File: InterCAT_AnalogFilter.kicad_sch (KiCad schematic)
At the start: 37 parts, among them T1 Transformer_1P_1S, T2 Transformer_1P_1S, T3 Transformer_1P_1S, T4 Transformer_1P_1S, U4 MCP6002, U5 MCP6002, U6 MCP6002

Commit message: added footprints for trimmers and trasf
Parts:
- RV1, RV2, RV3, RV4: footprint (none) -> Potentiometer_THT:Potentiometer_Bourns_3386P_Vertical
- T1, T2, T3, T4: footprint (none) -> InterCat:LM-NP-1001-B1L
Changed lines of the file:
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@@
       (effects (font (size 1.27 1.27)))
     )
-    (property "Footprint" "" (at 226.06 48.26 0)
+    (property "Footprint" "Potentiometer_THT:Potentiometer_Bourns_3386P_Vertical" (at 226.06 48.26 0)
       (effects (font (size 1.27 1.27)) hide)
     )
@@
       (effects (font (size 1.27 1.27)))
     )
-    (property "Footprint" "" (at 127 43.18 0)
+    (property "Footprint" "InterCat:LM-NP-1001-B1L" (at 127 43.18 0)
       (effects (font (size 1.27 1.27)) hide)
     )
@@
       (effects (font (size 1.27 1.27)))
     )
-    (property "Footprint" "" (at 93.98 101.6 0)
+    (property "Footprint" "Potentiometer_THT:Potentiometer_Bourns_3386P_Vertical" (at 93.98 101.6 0)
       (effects (font (size 1.27 1.27)) hide)
     )
@@
       (effects (font (size 1.27 1.27)))
     )
-    (property "Footprint" "" (at 179.07 101.6 0)
+    (property "Footprint" "InterCat:LM-NP-1001-B1L" (at 179.07 101.6 0)
       (effects (font (size 1.27 1.27)) hide)
     )
@@
       (effects (font (size 1.27 1.27)))
     )
-    (property "Footprint" "" (at 180.34 43.18 0)
+    (property "Footprint" "InterCat:LM-NP-1001-B1L" (at 180.34 43.18 0)
       (effects (font (size 1.27 1.27)) hide)
     )
@@
       (effects (font (size 1.27 1.27)))
     )
-    (property "Footprint" "" (at 224.79 106.68 0)
+    (property "Footprint" "Potentiometer_THT:Potentiometer_Bourns_3386P_Vertical" (at 224.79 106.68 0)
       (effects (font (size 1.27 1.27)) hide)
     )
@@
       (effects (font (size 1.27 1.27)))
     )
-    (property "Footprint" "" (at 93.98 39.37 0)
+    (property "Footprint" "Potentiometer_THT:Potentiometer_Bourns_3386P_Vertical" (at 93.98 39.37 0)
       (effects (font (size 1.27 1.27)) hide)
     )
@@
       (effects (font (size 1.27 1.27)))
     )
-    (property "Footprint" "" (at 127 105.41 0)
-      (effects (font (size 1.27 1.27)) hide)
-    )
+    (property "Footprint" "InterCat:LM-NP-1001-B1L" (at 127 105.41 0)
+      (effects (font (size 1.27 1.27)) hide)
+    )

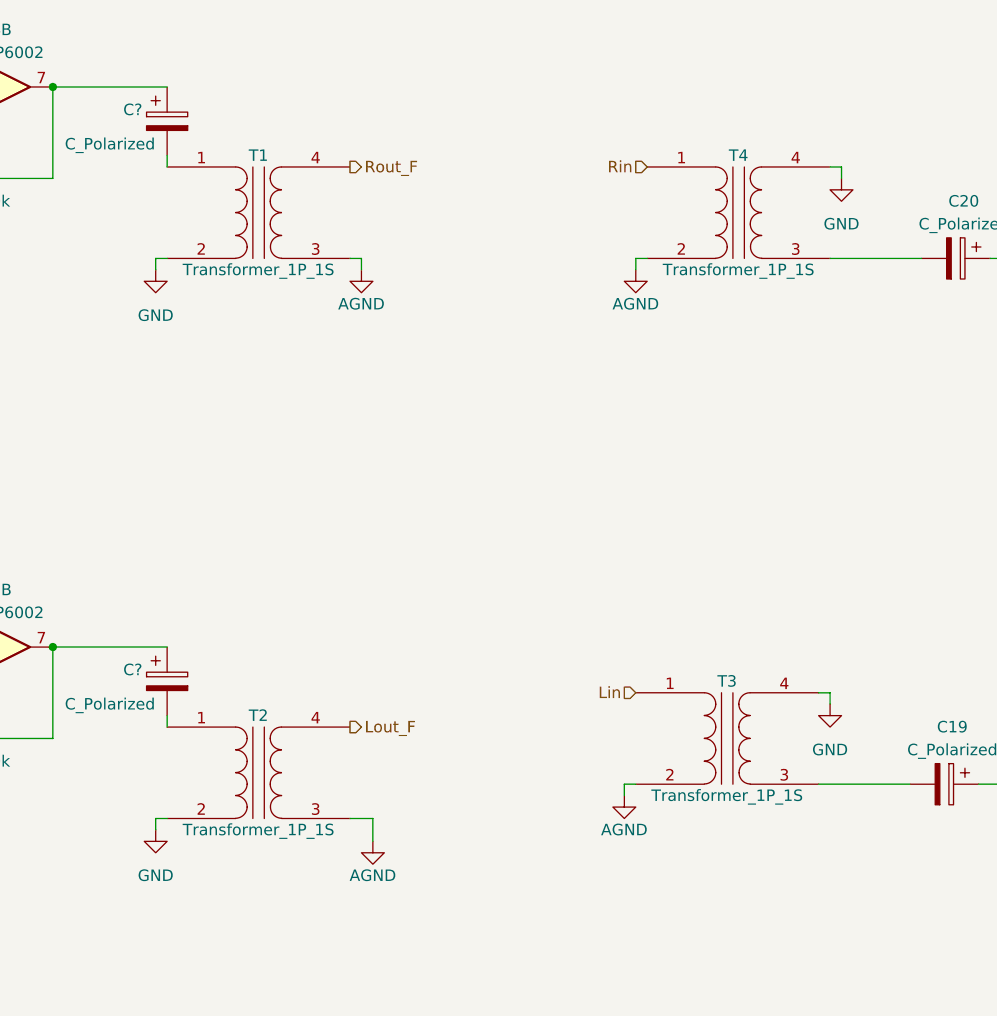
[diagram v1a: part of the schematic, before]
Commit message: corrected footprint AND symbol of trasf
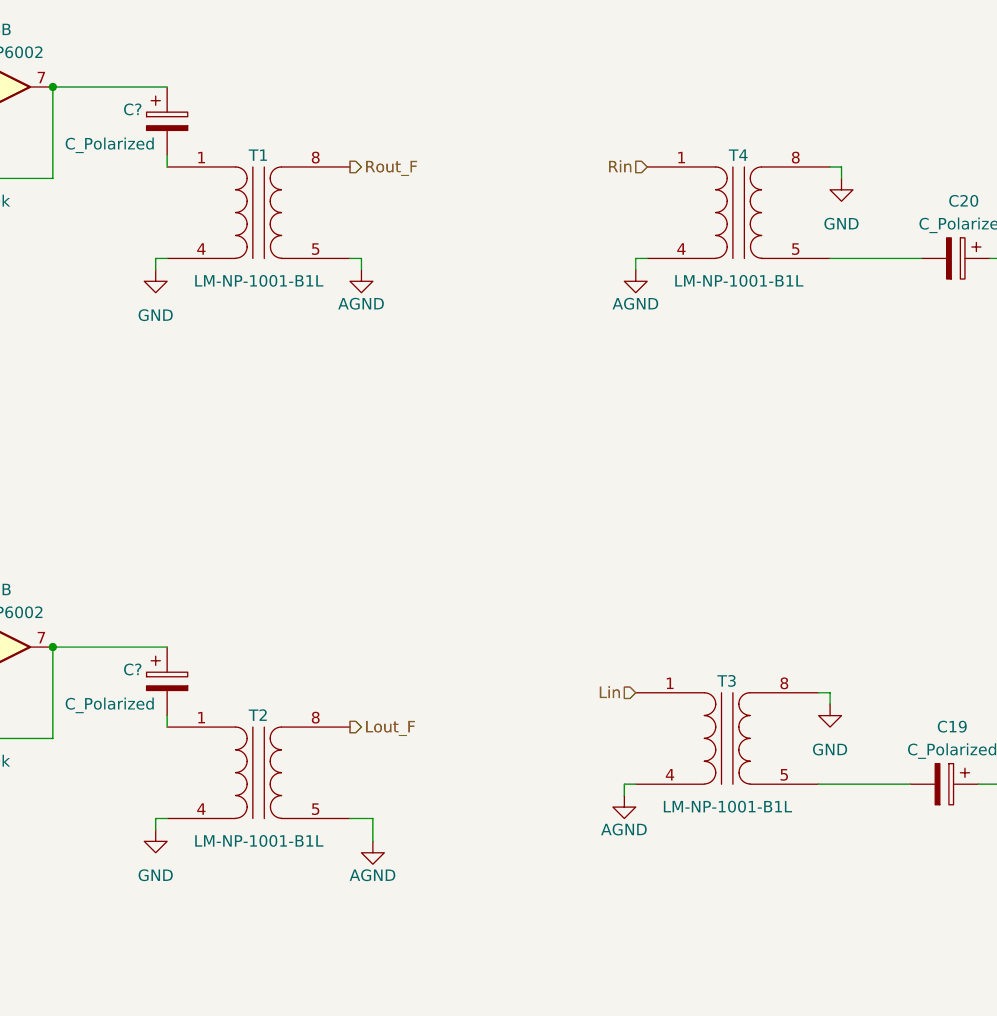
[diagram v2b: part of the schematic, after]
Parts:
- T1, T2, T3, T4: value Transformer_1P_1S -> LM-NP-1001-B1L; symbol Device:Transformer_1P_1S -> InterCat:LM-NP-1001-B1L
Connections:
- net GND: now also T1.4 (AB), T2.4 (AB), T3.8 (SB), T4.8 (SB); no longer T1.2 (AB), T2.2 (AB), T3.4 (SB), T4.4 (SB)
- net GNDA: now also T1.5 (SA), T2.5 (SA), T3.4 (AB), T4.4 (AB); no longer T1.3 (SA), T2.3 (SA), T3.2 (AB), T4.2 (AB)
- net Lout_F: now also T2.8 (SB); no longer T2.4 (SB)
- net Rout_F: now also T1.8 (SB); no longer T1.4 (SB)
- net at C20.2: now also T4.5 (SA); no longer T4.3 (SA)
- net at C19.2: now also T3.5 (SA); no longer T3.3 (SA)
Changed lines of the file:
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@@
     )
   )
-  (symbol (lib_id "Device:Transformer_1P_1S") (at 127 43.18 0) (unit 1)
+  (symbol (lib_id "InterCat:LM-NP-1001-B1L") (at 127 43.18 0) (unit 1)
     (in_bom yes) (on_board yes) (dnp no)
     (property "Reference" "T1" (at 127 36.83 0)
       (effects (font (size 1.27 1.27)))
     )
-    (property "Value" "Transformer_1P_1S" (at 127 49.53 0)
-      (effects (font (size 1.27 1.27)))
-    )
-    (property "Footprint" "InterCat:LM-NP-1001-B1L" (at 127 43.18 0)
-      (effects (font (size 1.27 1.27)) hide)
-    )
-    (property "Datasheet" "~" (at 127 43.18 0)
+    (property "Value" "LM-NP-1001-B1L" (at 127 50.8 0)
+      (effects (font (size 1.27 1.27)))
+    )
+    (property "Footprint" "InterCat:LM-NP-1001-B1L" (at 125.73 43.18 0)
+      (effects (font (size 1.27 1.27)) hide)
+    )
+    (property "Datasheet" "https://www.bourns.com/pdfs/LMNPLP.pdf" (at 127 43.18 0)
       (effects (font (size 1.27 1.27)) hide)
     )
@@
     )
     (pin "1")
-    (pin "2")
-    (pin "3")
     (pin "4")
+    (pin "5")
+    (pin "8")
     (instances
       (project "Intercat"
@@
     )
   )
-  (symbol (lib_id "Device:Transformer_1P_1S") (at 179.07 101.6 0) (unit 1)
+  (symbol (lib_id "InterCat:LM-NP-1001-B1L") (at 179.07 101.6 0) (unit 1)
     (in_bom yes) (on_board yes) (dnp no)
     (property "Reference" "T3" (at 179.07 95.25 0)
       (effects (font (size 1.27 1.27)))
     )
-    (property "Value" "Transformer_1P_1S" (at 179.07 107.95 0)
-      (effects (font (size 1.27 1.27)))
-    )
-    (property "Footprint" "InterCat:LM-NP-1001-B1L" (at 179.07 101.6 0)
-      (effects (font (size 1.27 1.27)) hide)
-    )
-    (property "Datasheet" "~" (at 179.07 101.6 0)
+    (property "Value" "LM-NP-1001-B1L" (at 179.07 109.22 0)
+      (effects (font (size 1.27 1.27)))
+    )
+    (property "Footprint" "InterCat:LM-NP-1001-B1L" (at 177.8 101.6 0)
+      (effects (font (size 1.27 1.27)) hide)
+    )
+    (property "Datasheet" "https://www.bourns.com/pdfs/LMNPLP.pdf" (at 179.07 101.6 0)
       (effects (font (size 1.27 1.27)) hide)
     )
@@
     )
     (pin "1")
-    (pin "2")
-    (pin "3")
     (pin "4")
+    (pin "5")
+    (pin "8")
     (instances
       (project "Intercat"
@@
     )
   )
-  (symbol (lib_id "Device:Transformer_1P_1S") (at 180.34 43.18 0) (unit 1)
+  (symbol (lib_id "InterCat:LM-NP-1001-B1L") (at 180.34 43.18 0) (unit 1)
     (in_bom yes) (on_board yes) (dnp no)
     (property "Reference" "T4" (at 180.34 36.83 0)
       (effects (font (size 1.27 1.27)))
     )
-    (property "Value" "Transformer_1P_1S" (at 180.34 49.53 0)
-      (effects (font (size 1.27 1.27)))
-    )
-    (property "Footprint" "InterCat:LM-NP-1001-B1L" (at 180.34 43.18 0)
-      (effects (font (size 1.27 1.27)) hide)
-    )
-    (property "Datasheet" "~" (at 180.34 43.18 0)
+    (property "Value" "LM-NP-1001-B1L" (at 180.34 50.8 0)
+      (effects (font (size 1.27 1.27)))
+    )
+    (property "Footprint" "InterCat:LM-NP-1001-B1L" (at 179.07 43.18 0)
+      (effects (font (size 1.27 1.27)) hide)
+    )
+    (property "Datasheet" "https://www.bourns.com/pdfs/LMNPLP.pdf" (at 180.34 43.18 0)
       (effects (font (size 1.27 1.27)) hide)
     )
@@
     )
     (pin "1")
-    (pin "2")
-    (pin "3")
     (pin "4")
+    (pin "5")
+    (pin "8")
     (instances
       (project "Intercat"
@@
     )
   )
-  (symbol (lib_id "Device:Transformer_1P_1S") (at 127 105.41 0) (unit 1)
+  (symbol (lib_id "InterCat:LM-NP-1001-B1L") (at 127 105.41 0) (unit 1)
     (in_bom yes) (on_board yes) (dnp no)
     (property "Reference" "T2" (at 127 99.06 0)
       (effects (font (size 1.27 1.27)))
     )
-    (property "Value" "Transformer_1P_1S" (at 127 111.76 0)
-      (effects (font (size 1.27 1.27)))
-    )
-    (property "Footprint" "InterCat:LM-NP-1001-B1L" (at 127 105.41 0)
-      (effects (font (size 1.27 1.27)) hide)
-    )
-    (property "Datasheet" "~" (at 127 105.41 0)
+    (property "Value" "LM-NP-1001-B1L" (at 127 113.03 0)
+      (effects (font (size 1.27 1.27)))
+    )
+    (property "Footprint" "InterCat:LM-NP-1001-B1L" (at 125.73 105.41 0)
+      (effects (font (size 1.27 1.27)) hide)
+    )
+    (property "Datasheet" "https://www.bourns.com/pdfs/LMNPLP.pdf" (at 127 105.41 0)
       (effects (font (size 1.27 1.27)) hide)
     )
@@
     )
     (pin "1")
-    (pin "2")
-    (pin "3")
     (pin "4")
-    (instances
-      (project "Intercat"
+    (pin "5")
+    (pin "8")
+    (instances
+      (project "Intercat"
